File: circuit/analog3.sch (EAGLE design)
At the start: 77 parts, among them IC1 OP07C, IC2 74HC4052D, IC3 AD8603UJ, IC4 AD8221R, IC5 AD8221R, IC6 LM258, IC7 LM258

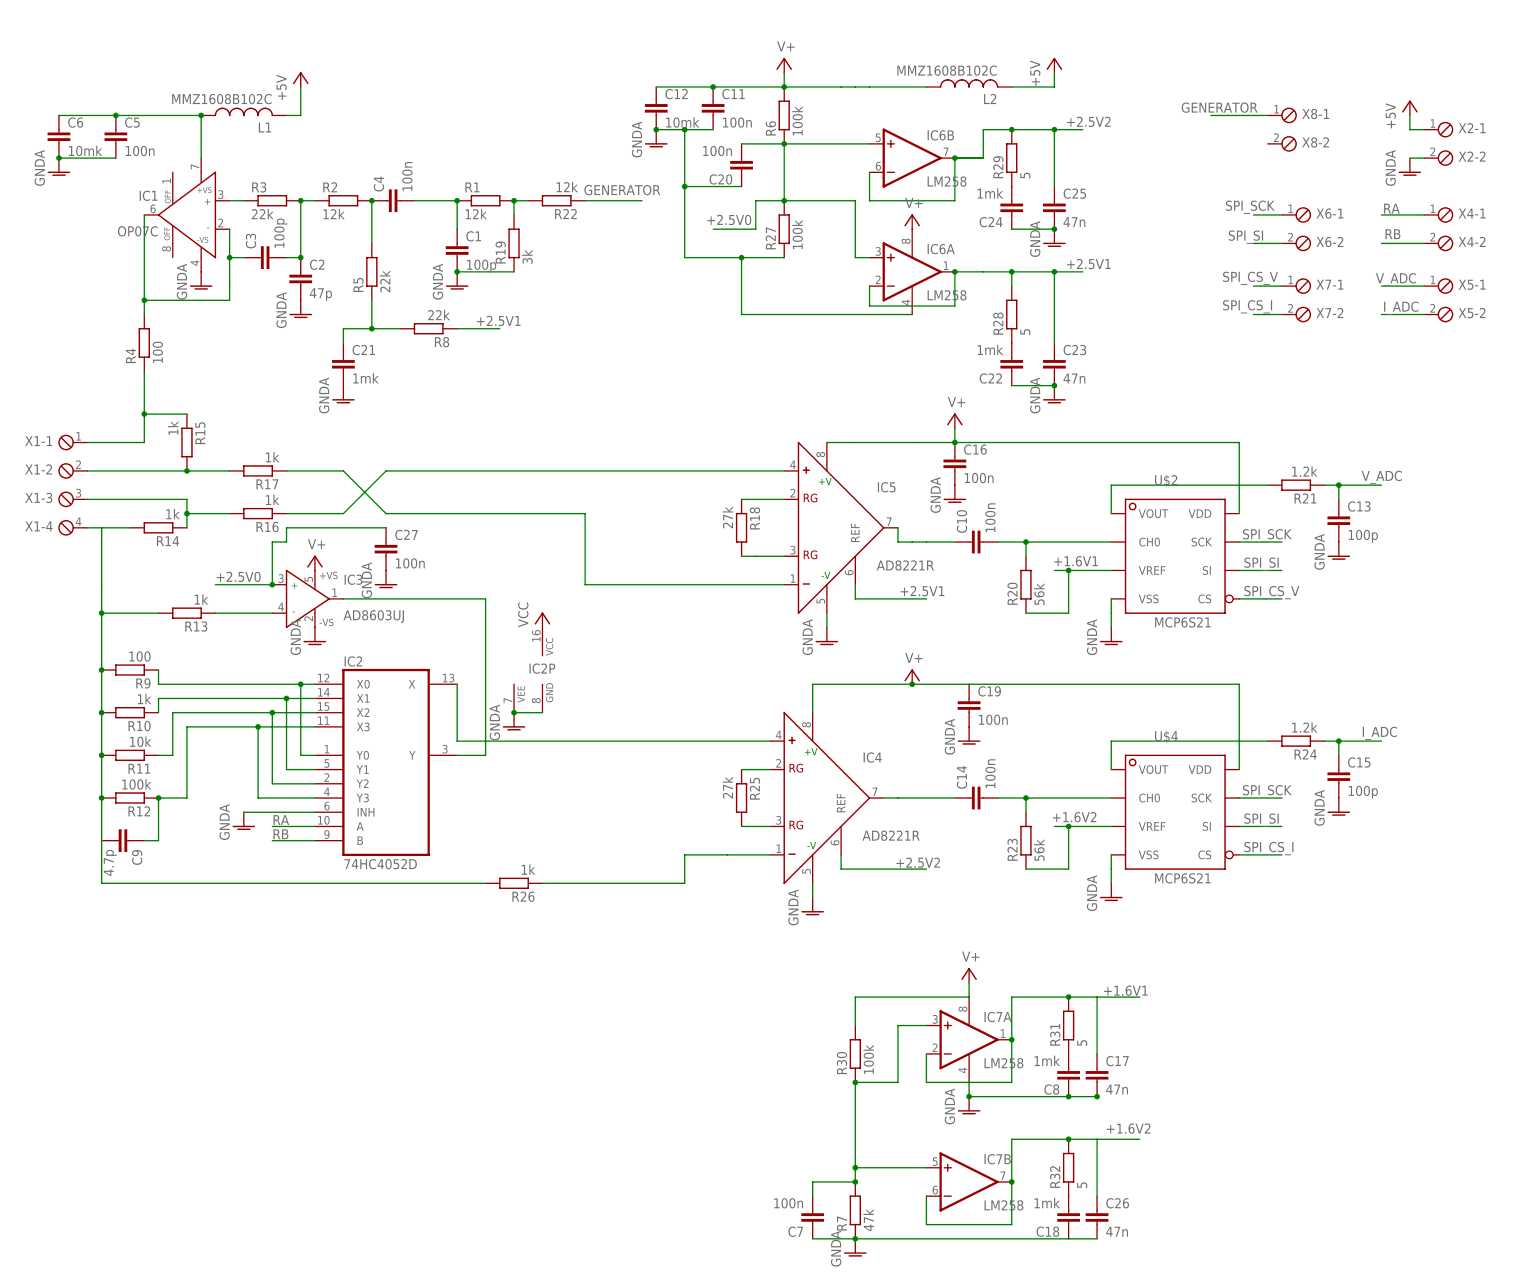
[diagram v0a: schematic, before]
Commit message: - переделали аналоговую часть под более быстрый усилитель -  убрали неработающие микроиндуктивности, поставили индуктивность побольше - подставили дополнительный конденсатор на +2.5V
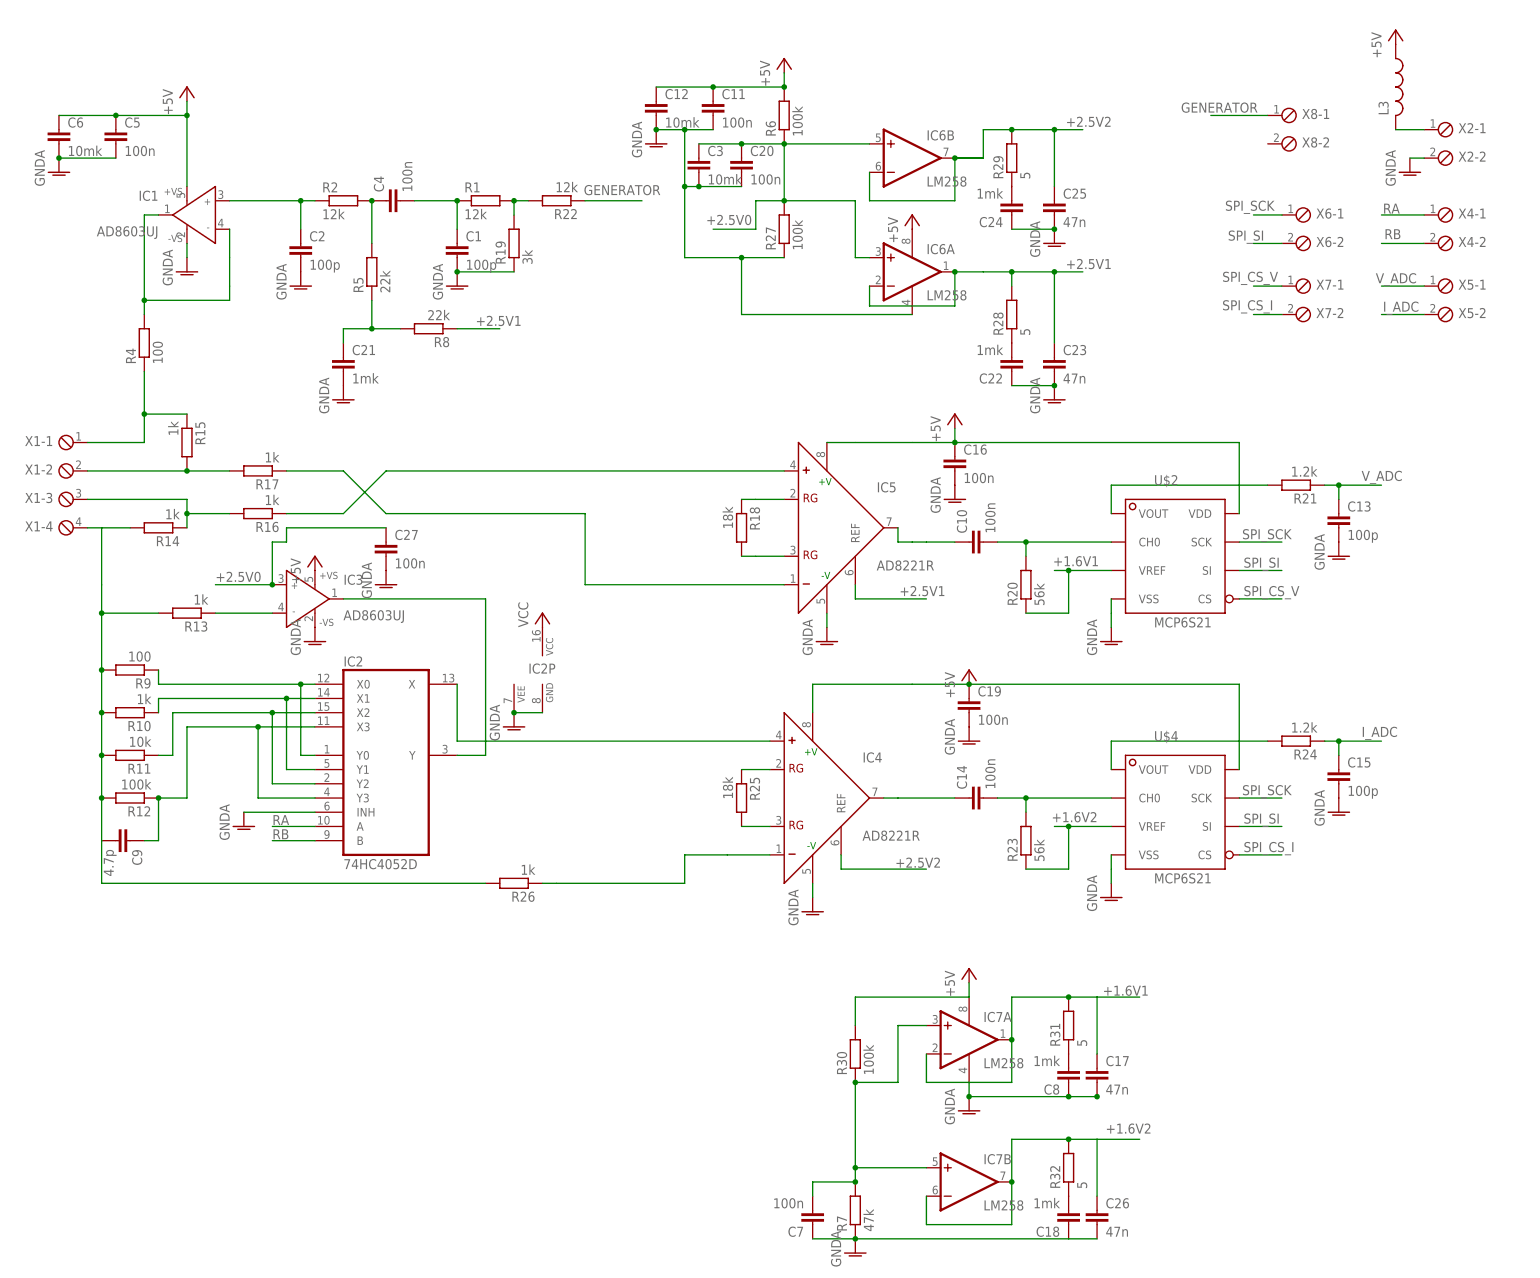
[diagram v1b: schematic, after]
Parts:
- removed L1, L2: MMZ1608B102C, rcl:L-US
- removed R3: 22k, rcl:R-EU_R0603
- added L3: (no value), rcl:L-US0204/7
- C2: value 47p -> 100p
- C3: value 100p -> 10mk
- IC1: value OP07C -> AD8603UJ; device analog-devices:AD817 -> analog-devices:AD8603UJ
- R18, R25: value 27k -> 18k
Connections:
- removed net N$7: C5.1, C6.1, IC1.+VS, L1.1
- removed net V+: C11.1, C12.1, C16.1, C19.1, IC3.+VS, IC4.+V, IC5.+V, IC6P.V+, IC7P.V+, L2.1, R30.2, R6.2, U$2.VDD, U$4.VDD
- net +2.5V0: now also C20.1, C3.1; no longer C20.2
- net +5V: now also C11.1, C12.1, C16.1, C19.1, C5.1, C6.1, IC1.+VS, IC3.+VS, IC4.+V, IC5.+V, IC6P.V+, IC7P.V+, L3.1, R30.2, R6.2, U$2.VDD, U$4.VDD; no longer L1.2, L2.2, X2-1.1
- net GNDA: now also C20.2, C3.2; no longer C20.1
- net N$3: now also IC1.IN+; no longer C3.2, R3.2
- net N$5: no longer C3.1
- net N$6: now also L3.2, X2-1.1; no longer IC1.IN+, R3.1
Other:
- moved on the sheet: C2, C20, C3

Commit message: - перед тем, как будем заводить SPI
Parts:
- removed C7: 100n, rcl:C-EUC0603
- removed R1: 12k, rcl:R-EU_R0603
- C1: value 100p -> 10mk
- C10, C14, C4: value 100n -> 1mk
- C13, C15: value 100p -> 150p
- R27, R6: value 100k -> 120k
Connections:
- removed net N$2: C1.1, C4.2, R1.1
- net GNDA: no longer C7.1
- net N$34: now also C4.2; no longer R1.2
- net N$41: now also C1.1; no longer C7.2
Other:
- moved on the sheet: C1
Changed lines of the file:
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@@
 </classes>
 <parts>
-<part name="R1" library="rcl" deviceset="R-EU_" device="R0603" value="12k"/>
-<part name="C1" library="rcl" deviceset="C-EU" device="C0805" value="100p"/>
 <part name="R2" library="rcl" deviceset="R-EU_" device="R0603" value="12k"/>
 <part name="C2" library="rcl" deviceset="C-EU" device="C0805" value="100p"/>
-<part name="C4" library="rcl" deviceset="C-EU" device="C0603" value="100n"/>
+<part name="C4" library="rcl" deviceset="C-EU" device="C0603" value="1mk"/>
 <part name="C5" library="rcl" deviceset="C-EU" device="C0603" value="100n"/>
 <part name="C6" library="rcl" deviceset="C-EU" device="C0805" value="10mk"/>
@@
 <part name="R5" library="rcl" deviceset="R-EU_" device="R0603" value="22k"/>
 <part name="P+3" library="supply1" deviceset="+5V" device=""/>
-<part name="R6" library="rcl" deviceset="R-EU_" device="R0603" value="100k"/>
+<part name="R6" library="rcl" deviceset="R-EU_" device="R0603" value="120k"/>
 <part name="R9" library="rcl" deviceset="R-EU_" device="R0603" value="100"/>
 <part name="R10" library="rcl" deviceset="R-EU_" device="R0603" value="1k"/>
@@
 <part name="R18" library="rcl" deviceset="R-EU_" device="R0603" value="18k"/>
 <part name="U$2" library="balmer" deviceset="MCP6S21" device=""/>
-<part name="C10" library="rcl" deviceset="C-EU" device="C0603" value="100n"/>
+<part name="C10" library="rcl" deviceset="C-EU" device="C0603" value="1mk"/>
 <part name="R20" library="rcl" deviceset="R-EU_" device="R0603" value="56k"/>
 <part name="GND9" library="supply1" deviceset="GNDA" device=""/>
@@
 <part name="GND11" library="supply1" deviceset="GNDA" device=""/>
 <part name="R21" library="rcl" deviceset="R-EU_" device="R0603" value="1.2k"/>
-<part name="C13" library="rcl" deviceset="C-EU" device="C0805" value="100p"/>
+<part name="C13" library="rcl" deviceset="C-EU" device="C0805" value="150p"/>
 <part name="GND13" library="supply1" deviceset="GNDA" device=""/>
 <part name="GND14" library="supply1" deviceset="GNDA" device=""/>
 <part name="GND12" library="supply1" deviceset="GNDA" device=""/>
 <part name="U$4" library="balmer" deviceset="MCP6S21" device=""/>
-<part name="C14" library="rcl" deviceset="C-EU" device="C0603" value="100n"/>
+<part name="C14" library="rcl" deviceset="C-EU" device="C0603" value="1mk"/>
 <part name="R23" library="rcl" deviceset="R-EU_" device="R0603" value="56k"/>
 <part name="GND15" library="supply1" deviceset="GNDA" device=""/>
 <part name="R24" library="rcl" deviceset="R-EU_" device="R0603" value="1.2k"/>
-<part name="C15" library="rcl" deviceset="C-EU" device="C0805" value="100p"/>
+<part name="C15" library="rcl" deviceset="C-EU" device="C0805" value="150p"/>
 <part name="GND16" library="supply1" deviceset="GNDA" device=""/>
 <part name="R25" library="rcl" deviceset="R-EU_" device="R0603" value="18k"/>
@@
 <part name="IC4" library="balmer" deviceset="AD8221" device="R"/>
 <part name="IC5" library="balmer" deviceset="AD8221" device="R"/>
-<part name="R27" library="rcl" deviceset="R-EU_" device="R0603" value="100k"/>
+<part name="R27" library="rcl" deviceset="R-EU_" device="R0603" value="120k"/>
 <part name="IC6" library="linear" deviceset="LM358" device="D" value="LM258"/>
 <part name="R28" library="rcl" deviceset="R-EU_" device="R0805" value="5"/>
@@
 <part name="R30" library="rcl" deviceset="R-EU_" device="R0603" value="100k"/>
 <part name="GND17" library="supply1" deviceset="GNDA" device=""/>
-<part name="C7" library="rcl" deviceset="C-EU" device="C0603" value="100n"/>
 <part name="R31" library="rcl" deviceset="R-EU_" device="R0805" value="5"/>
 <part name="C8" library="rcl" deviceset="C-EU" device="C0603" value="1mk"/>
@@
 <part name="P+8" library="supply1" deviceset="+5V" device=""/>
 <part name="P+9" library="supply1" deviceset="+5V" device=""/>
+<part name="C1" library="rcl" deviceset="C-EU" device="C0805" value="10mk"/>
 </parts>
 <sheets>
@@
 </plain>
 <instances>
-<instance part="R1" gate="G$1" x="10.16" y="78.74"/>
-<instance part="C1" gate="G$1" x="5.08" y="71.12"/>
 <instance part="R2" gate="G$1" x="-15.24" y="78.74"/>
 <instance part="C2" gate="G$1" x="-22.86" y="71.12"/>
@@
 <instance part="X5" gate="-2" x="180.34" y="58.42"/>
 <instance part="P+7" gate="1" x="172.72" y="109.22"/>
-<instance part="GND1" gate="1" x="5.08" y="63.5"/>
+<instance part="GND1" gate="1" x="15.24" y="63.5"/>
 <instance part="GND2" gate="1" x="-22.86" y="63.5"/>
 <instance part="GND3" gate="1" x="-43.18" y="66.04"/>
@@
 <instance part="R30" gate="G$1" x="76.2" y="-73.66" rot="R90"/>
 <instance part="GND17" gate="1" x="96.52" y="-83.82"/>
-<instance part="C7" gate="G$1" x="68.58" y="-104.14" rot="R180"/>
 <instance part="R31" gate="G$1" x="114.3" y="-68.58" rot="R90"/>
 <instance part="C8" gate="G$1" x="114.3" y="-78.74" rot="R180"/>
@@
 <instance part="P+4" gate="1" x="96.52" y="-5.08"/>
 <instance part="P+5" gate="1" x="96.52" y="-58.42"/>
-<instance part="P+8" gate="1" x="-20.32" y="15.24"/>
+<instance part="P+8" gate="1" x="-20.32" y="17.78"/>
 <instance part="P+9" gate="1" x="86.36" y="76.2"/>
+<instance part="C1" gate="G$1" x="63.5" y="-101.6"/>
 </instances>
 <busses>
 </busses>
 <nets>
-<net name="N$2" class="0">
-<segment>
-<pinref part="C1" gate="G$1" pin="1"/>
-<pinref part="R1" gate="G$1" pin="1"/>
-<wire x1="5.08" y1="73.66" x2="5.08" y2="78.74" width="0.1524" layer="91"/>
-<pinref part="C4" gate="G$1" pin="2"/>
-<wire x1="5.08" y1="78.74" x2="-2.54" y2="78.74" width="0.1524" layer="91"/>
-<junction x="5.08" y="78.74"/>
-</segment>
-</net>
 <net name="N$3" class="0">
 <segment>
@@
 <pinref part="IC3" gate="G$1" pin="+VS"/>
 <pinref part="P+8" gate="1" pin="+5V"/>
+<wire x1="-20.32" y1="15.24" x2="-20.32" y2="12.7" width="0.1524" layer="91"/>
 </segment>
 <segment>
@@
 </segment>
 <segment>
-<pinref part="C1" gate="G$1" pin="2"/>
 <pinref part="GND1" gate="1" pin="GNDA"/>
 <pinref part="R19" gate="G$1" pin="1"/>
-<wire x1="15.24" y1="66.04" x2="5.08" y2="66.04" width="0.1524" layer="91"/>
-<junction x="5.08" y="66.04"/>
 </segment>
 <segment>
@@
 </segment>
 <segment>
-<pinref part="C7" gate="G$1" pin="1"/>
 <pinref part="R7" gate="G$1" pin="1"/>
 <wire x1="68.58" y1="-106.68" x2="76.2" y2="-106.68" width="0.1524" layer="91"/>
@@
 <junction x="76.2" y="-106.68"/>
 <pinref part="GND18" gate="1" pin="GNDA"/>
+<pinref part="C1" gate="G$1" pin="2"/>
+<wire x1="63.5" y1="-106.68" x2="68.58" y2="-106.68" width="0.1524" layer="91"/>
 </segment>
 <segment>
@@
 <segment>
 <pinref part="R19" gate="G$1" pin="2"/>
-<pinref part="R1" gate="G$1" pin="2"/>
 <wire x1="15.24" y1="76.2" x2="15.24" y2="78.74" width="0.1524" layer="91"/>
 <pinref part="R22" gate="G$1" pin="2"/>
 <wire x1="17.78" y1="78.74" x2="15.24" y2="78.74" width="0.1524" layer="91"/>
+<pinref part="C4" gate="G$1" pin="2"/>
+<wire x1="15.24" y1="78.74" x2="-2.54" y2="78.74" width="0.1524" layer="91"/>
 <junction x="15.24" y="78.74"/>
 </segment>
@@
 <net name="N$41" class="0">
 <segment>
-<pinref part="C7" gate="G$1" pin="2"/>
-<wire x1="68.58" y1="-99.06" x2="68.58" y2="-96.52" width="0.1524" layer="91"/>
 <wire x1="68.58" y1="-96.52" x2="76.2" y2="-96.52" width="0.1524" layer="91"/>
 <pinref part="IC7" gate="A" pin="+IN"/>
@@
 <junction x="76.2" y="-93.98"/>
 <junction x="76.2" y="-78.74"/>
-</segment>
-</net>
+<pinref part="C1" gate="G$1" pin="1"/>
+<wire x1="68.58" y1="-96.52" x2="63.5" y2="-96.52" width="0.1524" layer="91"/>
+<wire x1="63.5" y1="-96.52" x2="63.5" y2="-99.06" width="0.1524" layer="91"/>
+</segment>
+</net>

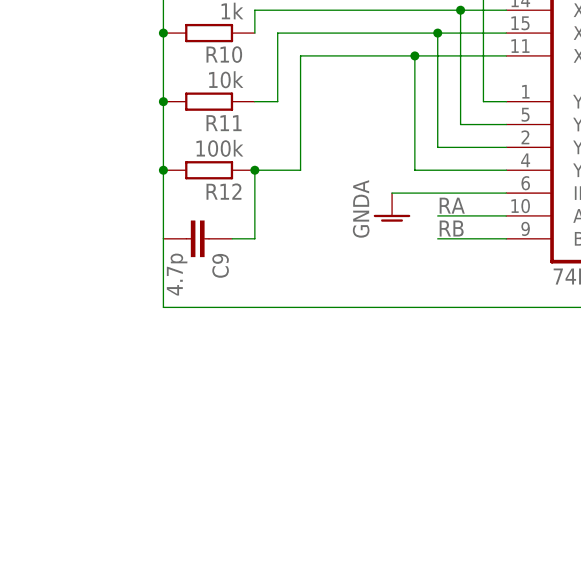
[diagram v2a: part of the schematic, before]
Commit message: - версия, которая почти успевает считать sin, cos свертку
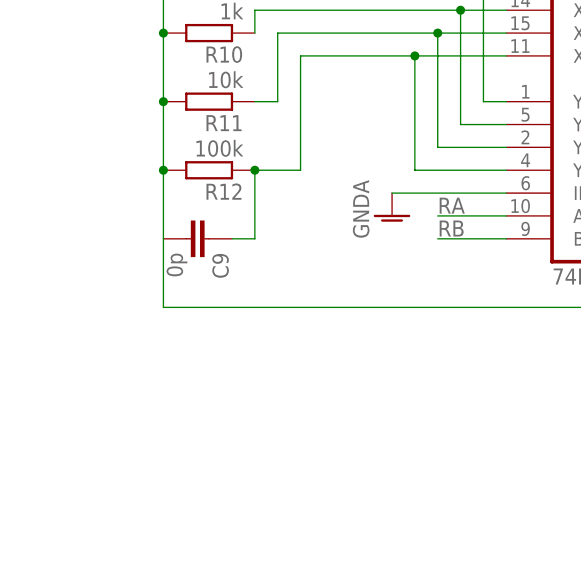
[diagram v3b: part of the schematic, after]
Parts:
- C9: value 4.7p -> 0p
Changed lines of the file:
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@@
 <part name="R12" library="rcl" deviceset="R-EU_" device="R0603" value="100k"/>
 <part name="R13" library="rcl" deviceset="R-EU_" device="R0603" value="1k"/>
-<part name="C9" library="rcl" deviceset="C-EU" device="C0805" value="4.7p"/>
+<part name="C9" library="rcl" deviceset="C-EU" device="C0805" value="0p"/>
 <part name="X1" library="con-phoenix-254" deviceset="MPT4" device=""/>
 <part name="R14" library="rcl" deviceset="R-EU_" device="R0603" value="1k"/>

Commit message: C2 100 p -> 33 p R30 100 K -> 56 K - перенастроили соответственно уровни усиления
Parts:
- C2: value 100p -> 33p
- R30: value 100k -> 56k
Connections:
- net +1.6V1 renamed +2.2V1
- net +1.6V2 renamed +2.2V2
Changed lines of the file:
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@@
 <parts>
 <part name="R2" library="rcl" deviceset="R-EU_" device="R0603" value="12k"/>
-<part name="C2" library="rcl" deviceset="C-EU" device="C0805" value="100p"/>
+<part name="C2" library="rcl" deviceset="C-EU" device="C0805" value="33p"/>
 <part name="C4" library="rcl" deviceset="C-EU" device="C0603" value="1mk"/>
 <part name="C5" library="rcl" deviceset="C-EU" device="C0603" value="100n"/>
@@
 <part name="IC7" library="linear" deviceset="LM358" device="D" value="LM258"/>
 <part name="R7" library="rcl" deviceset="R-EU_" device="R0603" value="47k"/>
-<part name="R30" library="rcl" deviceset="R-EU_" device="R0603" value="100k"/>
+<part name="R30" library="rcl" deviceset="R-EU_" device="R0603" value="56k"/>
 <part name="GND17" library="supply1" deviceset="GNDA" device=""/>
 <part name="R31" library="rcl" deviceset="R-EU_" device="R0805" value="5"/>
@@
 </segment>
 </net>
-<net name="+1.6V1" class="0">
+<net name="+2.2V1" class="0">
 <segment>
 <pinref part="IC7" gate="A" pin="OUT"/>
@@
 </segment>
 </net>
-<net name="+1.6V2" class="0">
+<net name="+2.2V2" class="0">
 <segment>
 <pinref part="IC7" gate="B" pin="-IN"/>

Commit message: - перед коррекцией по трем параметрам
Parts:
- C18, C8: value 1mk -> 4.7mk
- R31, R32: value 5 -> 22
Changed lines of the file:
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@@
 <part name="R30" library="rcl" deviceset="R-EU_" device="R0603" value="56k"/>
 <part name="GND17" library="supply1" deviceset="GNDA" device=""/>
-<part name="R31" library="rcl" deviceset="R-EU_" device="R0805" value="5"/>
-<part name="C8" library="rcl" deviceset="C-EU" device="C0603" value="1mk"/>
+<part name="R31" library="rcl" deviceset="R-EU_" device="R0805" value="22"/>
+<part name="C8" library="rcl" deviceset="C-EU" device="C0603" value="4.7mk"/>
 <part name="C17" library="rcl" deviceset="C-EU" device="C0805" value="47n"/>
-<part name="R32" library="rcl" deviceset="R-EU_" device="R0805" value="5"/>
-<part name="C18" library="rcl" deviceset="C-EU" device="C0603" value="1mk"/>
+<part name="R32" library="rcl" deviceset="R-EU_" device="R0805" value="22"/>
+<part name="C18" library="rcl" deviceset="C-EU" device="C0603" value="4.7mk"/>
 <part name="C26" library="rcl" deviceset="C-EU" device="C0805" value="47n"/>
 <part name="GND18" library="supply1" deviceset="GNDA" device=""/>
